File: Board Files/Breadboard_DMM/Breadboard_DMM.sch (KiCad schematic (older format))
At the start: 14 parts, among them J101 Conn_02x03_Odd_Even, J102 Conn_02x03_Odd_Even, U101 MIC5365-3.3YD5

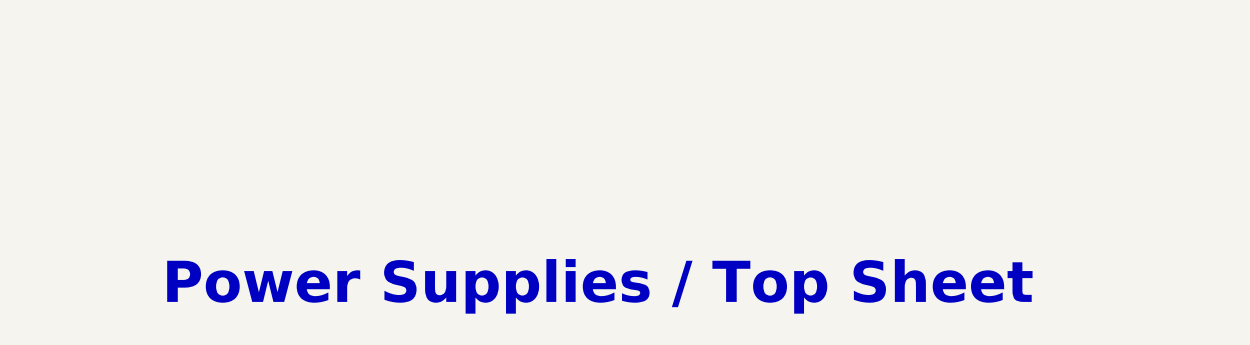
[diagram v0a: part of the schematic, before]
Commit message: Updated probe connector arrangement
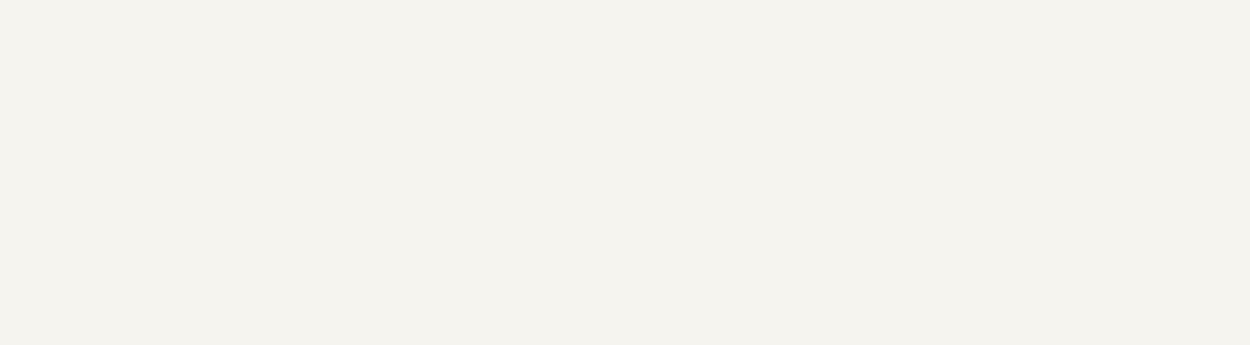
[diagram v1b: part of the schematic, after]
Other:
- note removed: "Power Supplies / Top Sheet"
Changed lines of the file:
@@
 Sheet 1 8
 Title "Toast-O-Meter"
-Date "2020-08-14"
+Date "2020-10-06"
 Rev "0"
 Comp ""
-Comment1 ""
+Comment1 "Isaac Rex"
 Comment2 ""
 Comment3 ""
@@
 	1    0    0    -1
 $EndComp
-Text Notes 12400 9750 0    180  ~ 36
-Power Supplies / Top Sheet
 Connection ~ 4500 1850
 Connection ~ 4500 2450

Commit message: Semi-finished component placement
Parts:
- removed J101, J102: Conn_02x03_Odd_Even, Connector_PinHeader_2.54mm:PinHeader_2x03_P2.54mm_Vertical, symbol Connector_Generic:Conn_02x03_Odd_Even
- added D101: Pink, irex_LED_SMD:LED_Kingbright_AA3528V_3.5x2.8mm_handsolder, symbol Device:LED_Filled
- added J101, J102: Conn_02x05_Odd_Even, Connector_PinHeader_2.54mm:PinHeader_2x05_P2.54mm_Vertical, symbol Connector_Generic:Conn_02x05_Odd_Even
- added R101: 1k, Resistor_SMD:R_0603_1608Metric_Pad1.05x0.95mm_HandSolder, symbol Device:R_US
- added SW101: L102021ML04Q, irex_Button_Switch_THT:SW_CuK_L102021ML04Q_SPDT_Angled, symbol Switch:SW_SPDT
- C101, C102, C104, C105: footprint Resistor_SMD:R_0805_2012Metric_Pad1.15x1.40mm_HandSolder -> Capacitor_SMD:C_0805_2012Metric_Pad1.18x1.45mm_HandSolder
- C103, C106: symbol Device:CP -> Device:C_Polarized
- C107, C108: footprint Resistor_SMD:R_0603_1608Metric_Pad1.05x0.95mm_HandSolder -> Capacitor_SMD:C_0603_1608Metric_Pad1.08x0.95mm_HandSolder
- L101, L102: footprint Inductor_SMD:L_0805_2012Metric_Pad1.15x1.40mm_HandSolder -> Inductor_SMD:L_Taiyo-Yuden_NR-30xx_HandSoldering; Digi-Key Link https://www.digikey.com/en/products/detail/tdk-corporation/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 -> https://www.digikey.com/en/products/detail/taiyo-yuden/NRH3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; Digi-Key PN 445-6761-1-ND -> 587-2592-1-ND
- PS101: MPN (none) -> PDME1-S5-S5-S
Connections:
- net labels added: GNDL, V_IN_ISOLATOR
- wire segments 107 -> 122
- no-connect marks 6 -> 11
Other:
- moved on the sheet: C101, C102, C104, C105, L101, PS101

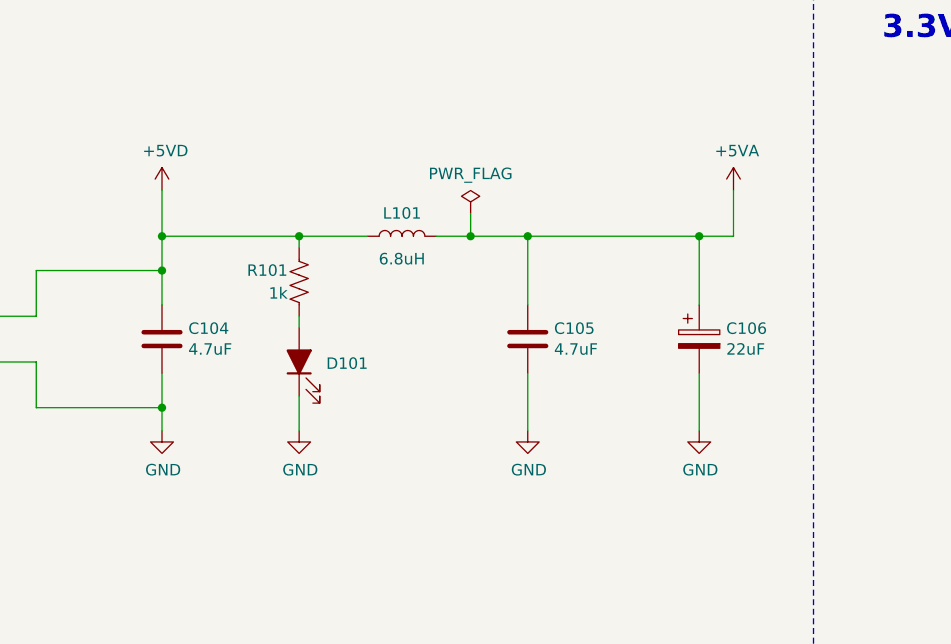
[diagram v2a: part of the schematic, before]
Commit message: Added silkscreen graphics and BOM
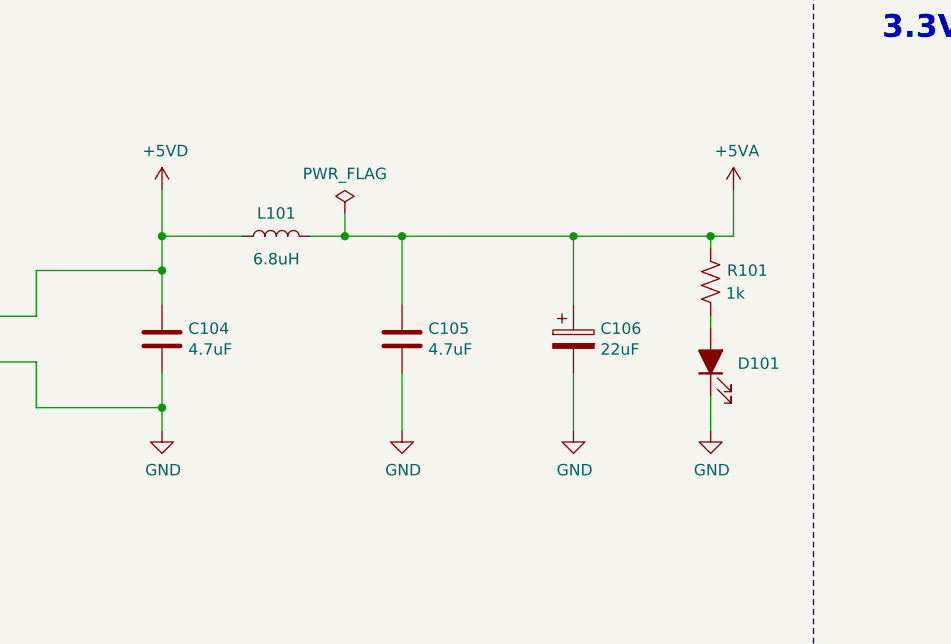
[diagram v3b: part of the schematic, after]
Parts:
- R101: Digi-Key Link https://www.digikey.com/en/products/detail/yageo/RC0603FR-0710KL/726880?s=N4IgTCBcDaIEoGEAMA2JBmAYnAtEg7AIxIDSAMiALoC%2BQA -> https://www.digikey.com/en/products/detail/yageo/RC0603FR-071KL/726843; Digi-Key PN 311-10.0KHRCT-ND -> 311-1.00KHRCT-ND
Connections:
- net +5VA: now also R101.1
- net +5VD: no longer R101.1
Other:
- moved on the sheet: C105, C106, D101, L101, R101

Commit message: Updated Digikey link for power isolator, started ADC driver
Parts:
- PS101: Digi-Key Link https://www.digikey.com/en/products/detail/cui-inc/PDME1-S5-D5-S/10229855 -> https://www.digikey.com/en/products/detail/cui-inc/PDME1-S5-S5-S/10229861?s=N4IgTCBcDaIAoBECyBRAjAWgMoFZt6xAF0BfIA
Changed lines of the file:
@@
 F 2 "irex_Converter_DCDC:CUI_DCDC-CONVERTER_PDME1-Sxx-S_1x4_P2.54mm_Drill1.0mm" H 7350 1900 50  0001 L CNN
 F 3 "https://www.cui.com/product/resource/pdme1-s.pdf" H 9450 1850 50  0001 L CNN
-F 4 "https://www.digikey.com/en/products/detail/cui-inc/PDME1-S5-D5-S/10229855" H 8400 2150 50  0001 C CNN "Digi-Key Link"
+F 4 "https://www.digikey.com/en/products/detail/cui-inc/PDME1-S5-S5-S/10229861?s=N4IgTCBcDaIAoBECyBRAjAWgMoFZt6xAF0BfIA" H 8400 2150 50  0001 C CNN "Digi-Key Link"
 F 5 "102-6320-ND" H 8400 2150 50  0001 C CNN "Digi-Key PN"
 F 6 "PDME1-S5-S5-S" H 8400 2150 50  0001 C CNN "MPN"
